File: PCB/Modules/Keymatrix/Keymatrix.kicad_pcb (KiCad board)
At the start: 2 copper layers, 29 x 59 mm, 21 parts, among them J1 Matrix1, J2 Matrix2, J3 In, U1 SP720ABTG

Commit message: Convert all KiCad to 6.0, clean up libraries, remove files that shouldn't be committed.
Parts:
- J3: footprint Custom:PinHeader_2x08_P2.54mm_Vertical-Centered -> KTANE:PinHeader_2x08_P2.54mm_Vertical-Centered
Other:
- net class Default removed
- net class v Power removed

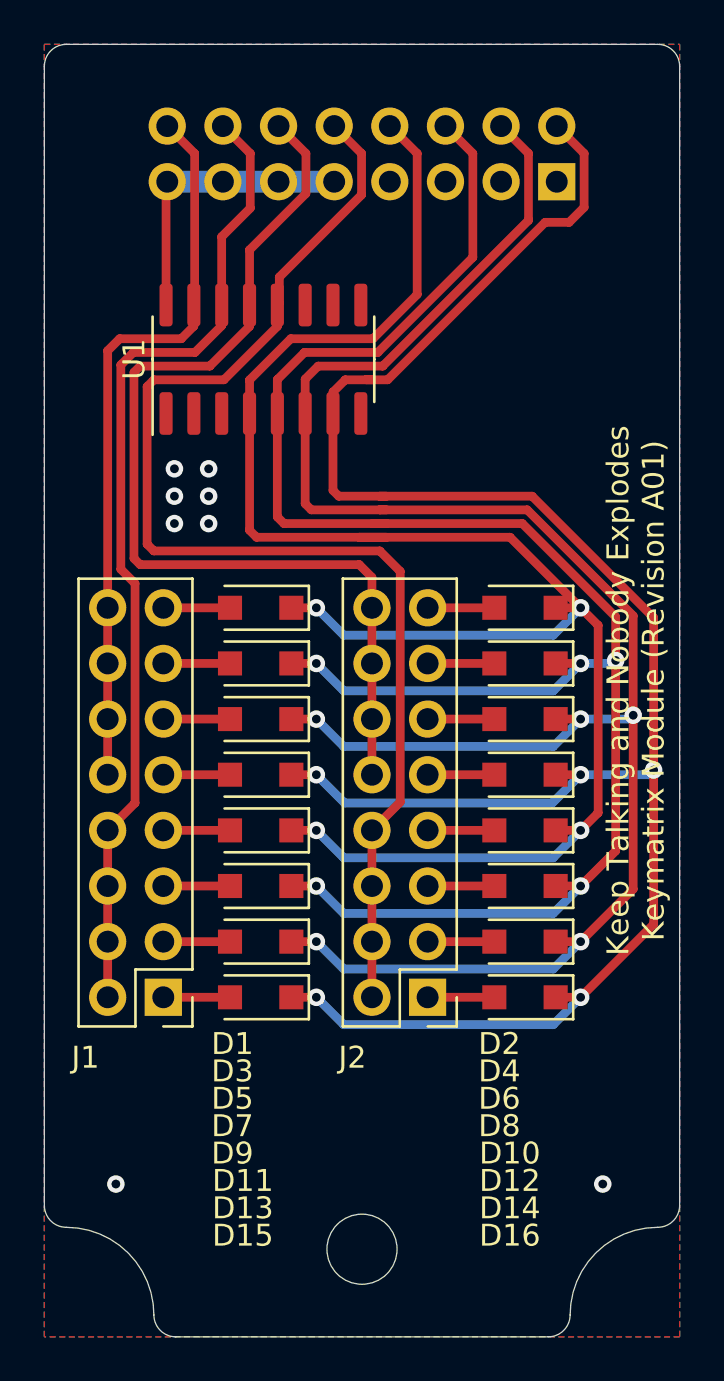
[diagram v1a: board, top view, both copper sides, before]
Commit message: Upgrade KiCad files from 6.0 to 7.0.
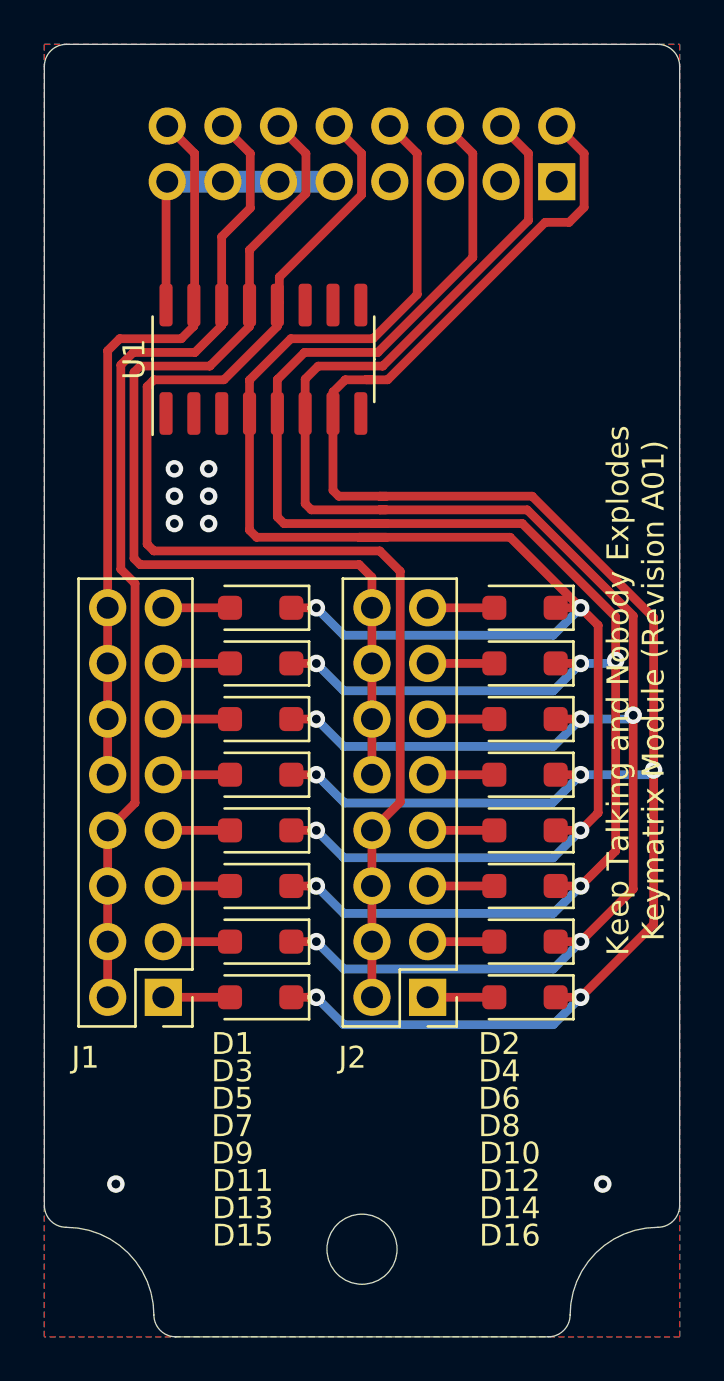
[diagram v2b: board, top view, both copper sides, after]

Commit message: First pass of PCB rework.
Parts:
- removed REF**: MountingHole_3.2mm_M3, MountingHole:MountingHole_3.2mm_M3
- added H1: MountingHole, MountingHole:MountingHole_3.2mm_M3, F.Cu at (34.5, 75.0)
- moved D8 15.8 mm to (29.8, 63.5)
- moved D9 15.8 mm to (41.9, 45.7)
- moved D6 14.3 mm to (29.8, 58.4)
- moved D11 14.2 mm to (41.9, 50.8)
- moved D4 13.1 mm to (29.8, 53.3)
- moved D13 13.1 mm to (41.9, 55.9)
- moved D2 12.4 mm to (29.8, 48.3)
- moved D15 12.3 mm to (41.9, 61.0)
- moved D7 7.62 mm to (29.8, 61.0)
- moved D10 7.62 mm to (41.9, 48.3)
- moved D5 5.08 mm to (29.8, 55.9)
- moved D12 5.08 mm to (41.9, 53.3)
- moved D14 2.54 mm to (41.9, 58.4)
- moved D3 2.54 mm to (29.8, 50.8)
- turned J3 to -90 degrees
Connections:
- D10 pad 1: ROW0 -> ROW1
- D10 pad 2: Net-(D10-Pad2) -> Net-(D10-A)
- D11 pad 1: ROW1 -> ROW2
- D11 pad 2: Net-(D11-Pad2) -> Net-(D11-A)
- D12 pad 1: ROW1 -> ROW3
- D12 pad 2: Net-(D12-Pad2) -> Net-(D12-A)
- D13 pad 1: ROW2 -> ROW0
- D13 pad 2: Net-(D13-Pad2) -> Net-(D13-A)
- D14 pad 1: ROW2 -> ROW1
- D14 pad 2: Net-(D14-Pad2) -> Net-(D14-A)
- D15 pad 1: ROW3 -> ROW2
- D15 pad 2: Net-(D15-Pad2) -> Net-(D15-A)
- D2 pad 1: ROW0 -> ROW1
- D2 pad 2: Net-(D2-Pad2) -> Net-(D2-A)
- D3 pad 1: ROW1 -> ROW2
- D3 pad 2: Net-(D3-Pad2) -> Net-(D3-A)
- D4 pad 1: ROW1 -> ROW3
- D4 pad 2: Net-(D4-Pad2) -> Net-(D4-A)
- D5 pad 1: ROW2 -> ROW0
- D5 pad 2: Net-(D5-Pad2) -> Net-(D5-A)
- D6 pad 1: ROW2 -> ROW1
- D6 pad 2: Net-(D6-Pad2) -> Net-(D6-A)
- D7 pad 1: ROW3 -> ROW2
- D7 pad 2: Net-(D7-Pad2) -> Net-(D7-A)
- D8 pad 2: Net-(D8-Pad2) -> Net-(D8-A)
- D9 pad 2: Net-(D9-Pad2) -> Net-(D9-A)
- J1 pad 1: Net-(D15-Pad2) -> Net-(D8-A)
- J1 pad 11: Net-(D5-Pad2) -> Net-(D3-A)
- J1 pad 13: Net-(D3-Pad2) -> Net-(D2-A)
- J1 pad 3: Net-(D13-Pad2) -> Net-(D7-A)
- J1 pad 5: Net-(D11-Pad2) -> Net-(D6-A)
- J1 pad 7: Net-(D9-Pad2) -> Net-(D5-A)
- J1 pad 9: Net-(D7-Pad2) -> Net-(D4-A)
- J2 pad 11: Net-(D6-Pad2) -> Net-(D11-A)
- J2 pad 13: Net-(D4-Pad2) -> Net-(D10-A)
- J2 pad 15: Net-(D2-Pad2) -> Net-(D9-A)
- J2 pad 3: Net-(D14-Pad2) -> Net-(D15-A)
- J2 pad 5: Net-(D12-Pad2) -> Net-(D14-A)
- J2 pad 7: Net-(D10-Pad2) -> Net-(D13-A)
- J2 pad 9: Net-(D8-Pad2) -> Net-(D12-A)
- J3 pad 1: GND -> COL0
- J3 pad 10: COL3 -> SPI-CLK
- J3 pad 11: +5V -> ROW1
- J3 pad 12: COL2 -> SPI-COPI
- J3 pad 13: +5V -> ROW2
- J3 pad 14: COL1 -> SPI-CIPO
- J3 pad 15: +5V -> ROW3
- J3 pad 16: COL0 -> GND
- J3 pad 2: ROW3 -> +5V
- J3 pad 3: GND -> COL1
- J3 pad 4: ROW2 -> +3.3V
- J3 pad 5: GND -> COL2
- J3 pad 6: ROW1 -> I2C-CLK
- J3 pad 7: GND -> COL3
- J3 pad 8: ROW0 -> I2C-DAT
- J3 pad 9: +5V -> ROW0
- U1 pad 16: +5V -> +3.3V
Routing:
- net +5V: track 13.3 -> 0.08 mm
- net +3.3V: track 0.00 -> 7.07 mm, vias 0 -> 1
- net Net-(D9-Pad2): track 3.05 -> 0.00 mm
- net Net-(D9-A): track 0.00 -> 3.05 mm
- net Net-(D8-Pad2): track 3.05 -> 0.00 mm
- net Net-(D8-A): track 0.00 -> 3.05 mm
- net Net-(D7-Pad2): track 3.05 -> 0.00 mm
- net Net-(D7-A): track 0.00 -> 3.05 mm
- net Net-(D6-Pad2): track 3.05 -> 0.00 mm
- net Net-(D6-A): track 0.00 -> 3.05 mm
- net Net-(D5-Pad2): track 3.05 -> 0.00 mm
- net Net-(D5-A): track 0.00 -> 3.05 mm
- net Net-(D4-Pad2): track 3.05 -> 0.00 mm
- net Net-(D4-A): track 0.00 -> 3.05 mm
- net Net-(D3-Pad2): track 3.05 -> 0.00 mm
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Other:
- board text added: "-"
- board text added: "Keep Talking and Nobody Explodes Keymatrix Module (Revision B01)"
- board text removed: "Keep Talking and Nobody Explodes Keymatrix Module (Revision A01)"
